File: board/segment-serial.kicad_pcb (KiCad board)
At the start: 2 copper layers, 69.8 x 40.6 mm, 20 parts, among them J1 Conn_01x07_Female, Q1 2N3906, Q2 2N3906, Q3 2N3906, Q4 2N3906, U1 74HC164, U2 CA56-12EWA, U3 74HC164

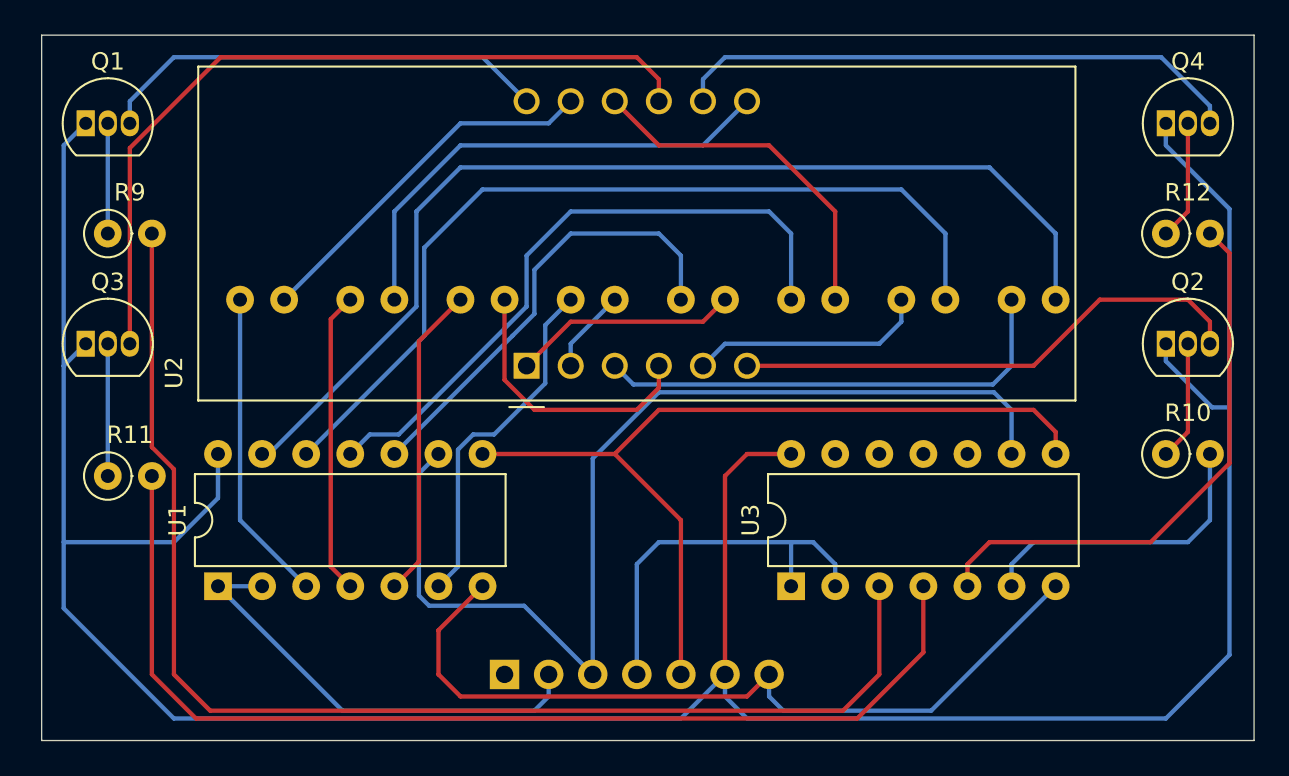
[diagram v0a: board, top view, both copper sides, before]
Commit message: Fixing issue with unconnected pins in U3
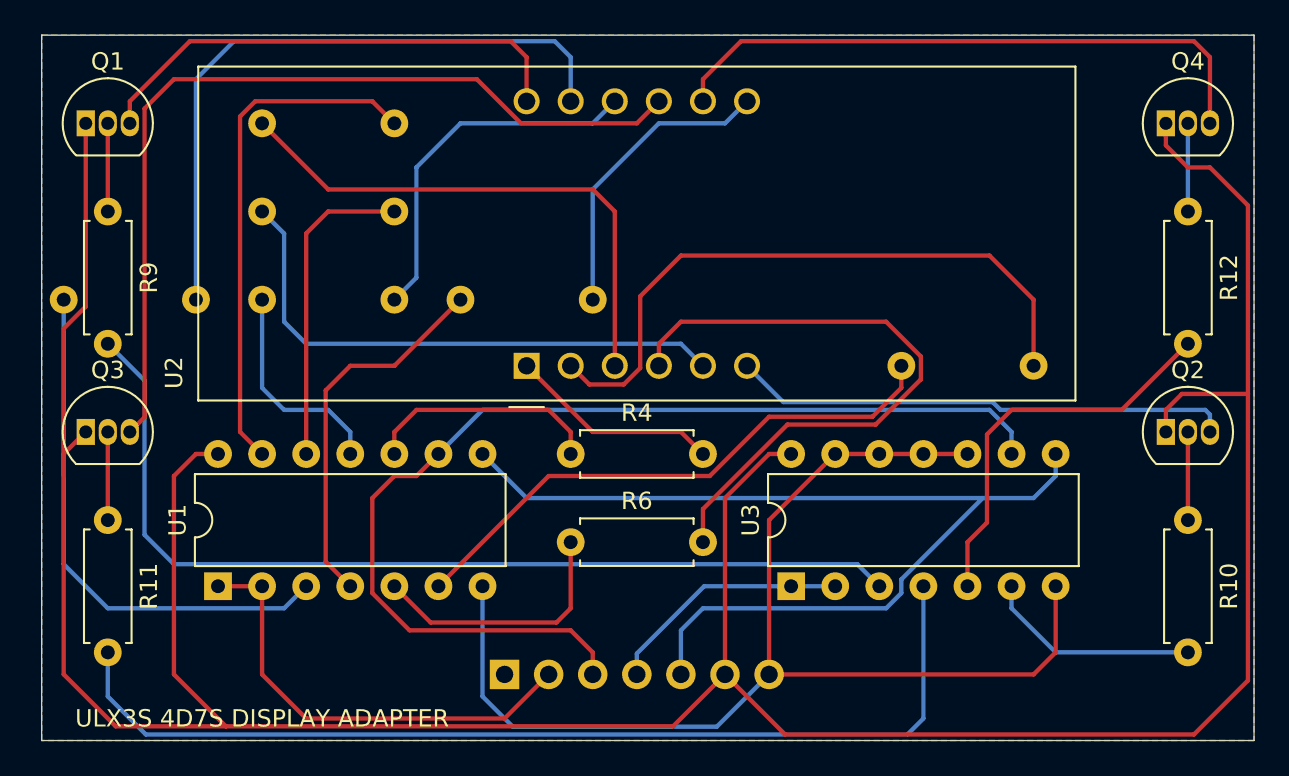
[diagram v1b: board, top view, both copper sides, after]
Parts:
- R1, R10, R11, R12, R2, R3, R5, R7, R8, R9: footprint Resistor_THT:R_Axial_DIN0207_L6.3mm_D2.5mm_P2.54mm_Vertical -> Resistor_THT:R_Axial_DIN0207_L6.3mm_D2.5mm_P7.62mm_Horizontal
- R4, R6: footprint Resistor_THT:R_Axial_DIN0207_L6.3mm_D2.5mm_P2.54mm_Vertical -> Resistor_THT:R_Axial_DIN0207_L6.3mm_D2.5mm_P7.62mm_Horizontal; moved to F.Cu
- moved R1 44.4 mm to (168.9, 41.9)
- moved R2 37.2 mm to (168.9, 47.0)
- moved R3 30.5 mm to (168.9, 52.1)
- moved R5 19.4 mm to (205.7, 55.9)
- moved R6 15.3 mm to (186.7, 66.0)
- moved R4 10.9 mm to (186.7, 61.0)
- moved R8 10.2 mm to (157.5, 52.1)
- moved R7 6.35 mm to (180.3, 52.1)
- moved Q2 5.08 mm to (221.0, 59.7)
- moved Q3 5.08 mm to (158.8, 59.7)
- moved R10 4.02 mm to (222.2, 64.8), turned to 270 degrees
- moved R11 2.54 mm to (160.0, 64.8), turned to 270 degrees
- moved R12 1.80 mm to (222.2, 47.0), turned to 270 degrees
- moved R9 1.27 mm to (160.0, 47.0), turned to 270 degrees
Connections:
- U3 pad 10: Net-(U3-Pad10) -> GND
- U3 pad 11: Net-(U3-Pad11) -> GND
- U3 pad 12: Net-(U3-Pad12) -> GND
- U3 pad 13: Net-(U3-Pad13) -> GND
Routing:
- net Net-(R2-Pad2): track 51.0 -> 18.3 mm
- net Net-(R5-Pad2): track 4.86 -> 37.5 mm
- net Net-(R1-Pad2): track 61.2 -> 29.7 mm
- net Net-(R3-Pad1): track 37.2 -> 12.5 mm
- net Net-(R6-Pad2): track 16.0 -> 36.6 mm
- net GND: track 47.3 -> 67.6 mm
- net Net-(R2-Pad1): track 13.8 -> 32.1 mm
- net /CA1: track 73.4 -> 55.4 mm
- net Net-(R8-Pad2): track 21.2 -> 38.1 mm
- net VCC: track 170.6 -> 183.7 mm
- net Net-(R8-Pad1): track 18.1 -> 30.8 mm
- net Net-(R4-Pad1): track 26.3 -> 13.8 mm
- net Net-(R5-Pad1): track 20.4 -> 32.7 mm
- net Net-(R7-Pad2): track 28.0 -> 17.3 mm
- net /CA3: track 32.5 -> 23.0 mm
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- added copper zone on B.Cu, net GND
- added copper zone on F.Cu, net GND
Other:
- board text added: "ULX3S 4D7S DISPLAY ADAPTER"
